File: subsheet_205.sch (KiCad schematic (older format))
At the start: 23 parts, among them U204 TL497A_DIP-14_500MA_PEAK_STEP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, U205 TL497A_DIP-14_500MA_PEAK_STEP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

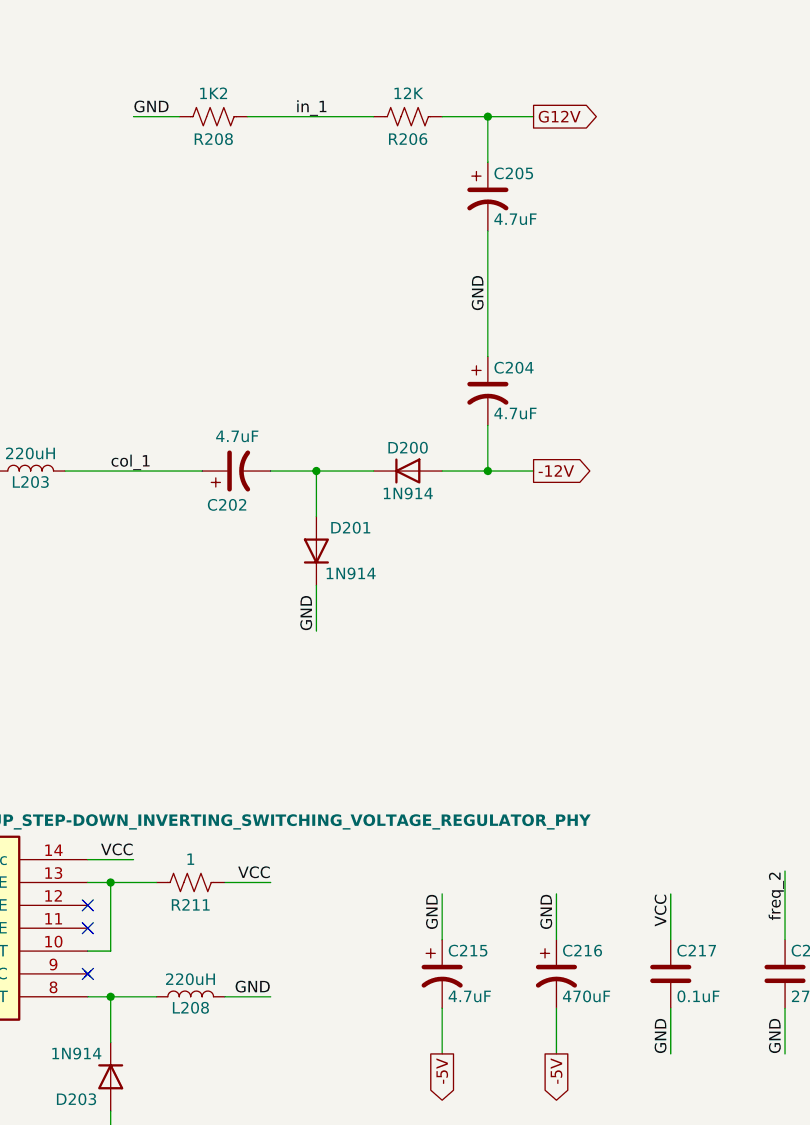
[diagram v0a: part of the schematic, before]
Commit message: Resolves #12 : Use the reference 'CP?' for polarized capacitors
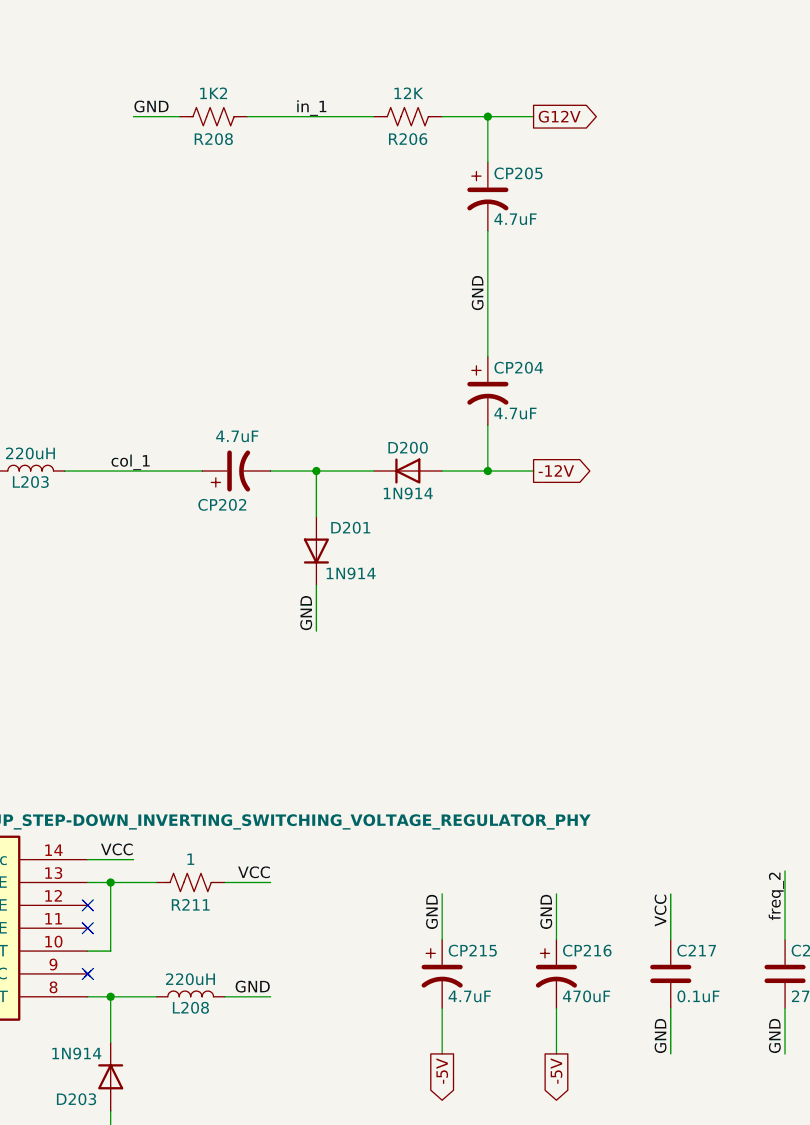
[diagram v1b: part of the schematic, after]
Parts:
- renumbered C202 to CP202, C204 to CP204, C205 to CP205, C215 to CP215, C216 to CP216
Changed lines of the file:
@@
 GND
 $Comp
-L Device:CP1 C205
+L Device:CP1 CP205
 U 1 1 609F4921
 P 5450 2850
-F 0 "C205" H 5475 2950 50  0000 L CNN
+F 0 "CP205" H 5475 2950 50  0000 L CNN
 F 1 "4.7uF" H 5475 2750 50  0000 L CNN
 F 2 "commons_passives_THT:Passive_THT_capacitor_polarized_W5.08mm_L17.78mm" H 5450 2850 50  0001 C CNN
@@
 $EndComp
 $Comp
-L Device:CP1 C204
+L Device:CP1 CP204
 U 1 1 609F43AA
 P 5450 3700
-F 0 "C204" H 5475 3800 50  0000 L CNN
+F 0 "CP204" H 5475 3800 50  0000 L CNN
 F 1 "4.7uF" H 5475 3600 50  0000 L CNN
 F 2 "commons_passives_THT:Passive_THT_capacitor_polarized_W5.08mm_L17.78mm" H 5450 3700 50  0001 C CNN
@@
 	3600 4050 4200 4050
 $Comp
-L Device:CP1 C202
+L Device:CP1 CP202
 U 1 1 609EE420
 P 4350 4050
-F 0 "C202" V 4200 4000 50  0000 L CNN
+F 0 "CP202" V 4200 4000 50  0000 L CNN
 F 1 "4.7uF" V 4500 3950 50  0000 L CNN
 F 2 "commons_passives_THT:Passive_THT_capacitor_polarized_W5.08mm_L17.78mm" H 4350 4050 50  0001 C CNN
@@
 GND
 $Comp
-L Device:CP1 C215
+L Device:CP1 CP215
 U 1 1 60A33402
 P 5250 6250
-F 0 "C215" H 5275 6350 50  0000 L CNN
+F 0 "CP215" H 5275 6350 50  0000 L CNN
 F 1 "4.7uF" H 5275 6150 50  0000 L CNN
 F 2 "commons_passives_THT:Passive_THT_capacitor_polarized_W5.08mm_L17.78mm" H 5250 6250 50  0001 C CNN
@@
 GND
 $Comp
-L Device:CP1 C216
+L Device:CP1 CP216
 U 1 1 60A37D1D
 P 5750 6250
-F 0 "C216" H 5775 6350 50  0000 L CNN
+F 0 "CP216" H 5775 6350 50  0000 L CNN
 F 1 "470uF" H 5775 6150 50  0000 L CNN
 F 2 "commons_passives_THT:Passive_THT_capacitor_polarized_W10.16mm_L27.94mm" H 5750 6250 50  0001 C CNN

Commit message: Resolves #13 : assign 1206 hand-solder footprints to resistors
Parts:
- R203, R206, R208, R211, R213, R214: footprint commons_passives_THT:Passive_THT_resistor_W2.54mm_L12.70mm -> Resistor_SMD:R_1206_3216Metric_Pad1.30x1.75mm_HandSolder
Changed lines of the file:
@@
 F 0 "R208" V 4350 2500 50  0000 C CNN
 F 1 "1K2" V 4150 2500 50  0000 C CNN
-F 2 "commons_passives_THT:Passive_THT_resistor_W2.54mm_L12.70mm" V 4290 2490 50  0001 C CNN
+F 2 "Resistor_SMD:R_1206_3216Metric_Pad1.30x1.75mm_HandSolder" V 4290 2490 50  0001 C CNN
 F 3 "~" H 4250 2500 50  0001 C CNN
 	1    4250 2500
@@
 F 0 "R206" V 5200 2500 50  0000 C CNN
 F 1 "12K" V 5000 2500 50  0000 C CNN
-F 2 "commons_passives_THT:Passive_THT_resistor_W2.54mm_L12.70mm" V 5140 2490 50  0001 C CNN
+F 2 "Resistor_SMD:R_1206_3216Metric_Pad1.30x1.75mm_HandSolder" V 5140 2490 50  0001 C CNN
 F 3 "~" H 5100 2500 50  0001 C CNN
 	1    5100 2500
@@
 F 0 "R203" V 2700 4050 50  0000 C CNN
 F 1 "5.1" V 2500 4050 50  0000 C CNN
-F 2 "commons_passives_THT:Passive_THT_resistor_W2.54mm_L12.70mm" V 2640 4040 50  0001 C CNN
+F 2 "Resistor_SMD:R_1206_3216Metric_Pad1.30x1.75mm_HandSolder" V 2640 4040 50  0001 C CNN
 F 3 "~" H 2600 4050 50  0001 C CNN
 	1    2600 4050
@@
 F 0 "R214" V 2700 7050 50  0000 C CNN
 F 1 "3K9" V 2500 7050 50  0000 C CNN
-F 2 "commons_passives_THT:Passive_THT_resistor_W2.54mm_L12.70mm" V 2640 7040 50  0001 C CNN
+F 2 "Resistor_SMD:R_1206_3216Metric_Pad1.30x1.75mm_HandSolder" V 2640 7040 50  0001 C CNN
 F 3 "~" H 2600 7050 50  0001 C CNN
 	1    2600 7050
@@
 F 0 "R213" V 3550 7050 50  0000 C CNN
 F 1 "1K2" V 3350 7050 50  0000 C CNN
-F 2 "commons_passives_THT:Passive_THT_resistor_W2.54mm_L12.70mm" V 3490 7040 50  0001 C CNN
+F 2 "Resistor_SMD:R_1206_3216Metric_Pad1.30x1.75mm_HandSolder" V 3490 7040 50  0001 C CNN
 F 3 "~" H 3450 7050 50  0001 C CNN
 	1    3450 7050
@@
 F 0 "R211" V 4250 5850 50  0000 C CNN
 F 1 "1" V 4050 5850 50  0000 C CNN
-F 2 "commons_passives_THT:Passive_THT_resistor_W2.54mm_L12.70mm" V 4190 5840 50  0001 C CNN
+F 2 "Resistor_SMD:R_1206_3216Metric_Pad1.30x1.75mm_HandSolder" V 4190 5840 50  0001 C CNN
 F 3 "~" H 4150 5850 50  0001 C CNN
 	1    4150 5850

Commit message: Resolves #8 : Assign 1206 hand-solder footprints to non polarized capacitors
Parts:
- C207, C217: footprint commons_passives_THT:Passive_THT_capacitor_mlcc_W2.54mm_L7.62mm -> Capacitor_SMD:C_1206_3216Metric_Pad1.33x1.80mm_HandSolder
- C208, C209, C218: footprint commons_passives_THT:Passive_THT_capacitor_W2.54mm_L10.16mm -> Capacitor_SMD:C_1206_3216Metric_Pad1.33x1.80mm_HandSolder
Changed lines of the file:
@@
 F 0 "C207" H 5425 1700 50  0000 L CNN
 F 1 "0.1uF" H 5425 1500 50  0000 L CNN
-F 2 "commons_passives_THT:Passive_THT_capacitor_mlcc_W2.54mm_L7.62mm" H 5438 1450 50  0001 C CNN
+F 2 "Capacitor_SMD:C_1206_3216Metric_Pad1.33x1.80mm_HandSolder" H 5438 1450 50  0001 C CNN
 F 3 "~" H 5400 1600 50  0001 C CNN
 	1    5400 1600
@@
 F 0 "C209" H 5925 1700 50  0000 L CNN
 F 1 "330pF" H 5925 1500 50  0000 L CNN
-F 2 "commons_passives_THT:Passive_THT_capacitor_W2.54mm_L10.16mm" H 5938 1450 50  0001 C CNN
+F 2 "Capacitor_SMD:C_1206_3216Metric_Pad1.33x1.80mm_HandSolder" H 5938 1450 50  0001 C CNN
 F 3 "~" H 5900 1600 50  0001 C CNN
 	1    5900 1600
@@
 F 0 "C208" H 2975 4500 50  0000 L CNN
 F 1 "150pF" H 2975 4300 50  0000 L CNN
-F 2 "commons_passives_THT:Passive_THT_capacitor_W2.54mm_L10.16mm" H 2988 4250 50  0001 C CNN
+F 2 "Capacitor_SMD:C_1206_3216Metric_Pad1.33x1.80mm_HandSolder" H 2988 4250 50  0001 C CNN
 F 3 "~" H 2950 4400 50  0001 C CNN
 	1    2950 4400
@@
 F 0 "C217" H 6275 6350 50  0000 L CNN
 F 1 "0.1uF" H 6275 6150 50  0000 L CNN
-F 2 "commons_passives_THT:Passive_THT_capacitor_mlcc_W2.54mm_L7.62mm" H 6288 6100 50  0001 C CNN
+F 2 "Capacitor_SMD:C_1206_3216Metric_Pad1.33x1.80mm_HandSolder" H 6288 6100 50  0001 C CNN
 F 3 "~" H 6250 6250 50  0001 C CNN
 	1    6250 6250
@@
 F 0 "C218" H 6775 6350 50  0000 L CNN
 F 1 "270pF" H 6775 6150 50  0000 L CNN
-F 2 "commons_passives_THT:Passive_THT_capacitor_W2.54mm_L10.16mm" H 6788 6100 50  0001 C CNN
+F 2 "Capacitor_SMD:C_1206_3216Metric_Pad1.33x1.80mm_HandSolder" H 6788 6100 50  0001 C CNN
 F 3 "~" H 6750 6250 50  0001 C CNN
 	1    6750 6250

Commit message: Resolves #9 : Assign radial THT footprints to polarized capacitors
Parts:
- CP202, CP204, CP205, CP215: footprint commons_passives_THT:Passive_THT_capacitor_polarized_W5.08mm_L17.78mm -> Capacitor_THT:C_Radial_D5.0mm_H11.0mm_P2.00mm
- CP216: footprint commons_passives_THT:Passive_THT_capacitor_polarized_W10.16mm_L27.94mm -> Capacitor_THT:C_Radial_D12.5mm_H20.0mm_P5.00mm
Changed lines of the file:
@@
 F 0 "CP205" H 5475 2950 50  0000 L CNN
 F 1 "4.7uF" H 5475 2750 50  0000 L CNN
-F 2 "commons_passives_THT:Passive_THT_capacitor_polarized_W5.08mm_L17.78mm" H 5450 2850 50  0001 C CNN
+F 2 "Capacitor_THT:C_Radial_D5.0mm_H11.0mm_P2.00mm" H 5450 2850 50  0001 C CNN
 F 3 "~" H 5450 2850 50  0001 C CNN
 	1    5450 2850
@@
 F 0 "CP204" H 5475 3800 50  0000 L CNN
 F 1 "4.7uF" H 5475 3600 50  0000 L CNN
-F 2 "commons_passives_THT:Passive_THT_capacitor_polarized_W5.08mm_L17.78mm" H 5450 3700 50  0001 C CNN
+F 2 "Capacitor_THT:C_Radial_D5.0mm_H11.0mm_P2.00mm" H 5450 3700 50  0001 C CNN
 F 3 "~" H 5450 3700 50  0001 C CNN
 	1    5450 3700
@@
 F 0 "CP202" V 4200 4000 50  0000 L CNN
 F 1 "4.7uF" V 4500 3950 50  0000 L CNN
-F 2 "commons_passives_THT:Passive_THT_capacitor_polarized_W5.08mm_L17.78mm" H 4350 4050 50  0001 C CNN
+F 2 "Capacitor_THT:C_Radial_D5.0mm_H11.0mm_P2.00mm" H 4350 4050 50  0001 C CNN
 F 3 "~" H 4350 4050 50  0001 C CNN
 	1    4350 4050
@@
 F 0 "CP215" H 5275 6350 50  0000 L CNN
 F 1 "4.7uF" H 5275 6150 50  0000 L CNN
-F 2 "commons_passives_THT:Passive_THT_capacitor_polarized_W5.08mm_L17.78mm" H 5250 6250 50  0001 C CNN
+F 2 "Capacitor_THT:C_Radial_D5.0mm_H11.0mm_P2.00mm" H 5250 6250 50  0001 C CNN
 F 3 "~" H 5250 6250 50  0001 C CNN
 	1    5250 6250
@@
 F 0 "CP216" H 5775 6350 50  0000 L CNN
 F 1 "470uF" H 5775 6150 50  0000 L CNN
-F 2 "commons_passives_THT:Passive_THT_capacitor_polarized_W10.16mm_L27.94mm" H 5750 6250 50  0001 C CNN
+F 2 "Capacitor_THT:C_Radial_D12.5mm_H20.0mm_P5.00mm" H 5750 6250 50  0001 C CNN
 F 3 "~" H 5750 6250 50  0001 C CNN
 	1    5750 6250

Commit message: Resolves #16 : assign smd footprints to diodes
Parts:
- D200, D201, D203: footprint commons_passives_THT:Passive_THT_diode_W2.54mm_L12.70mm -> Diode_SMD:D_SOD-123F
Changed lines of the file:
@@
 F 0 "D201" V 4800 4250 50  0000 C CNN
 F 1 "1N914" V 4600 4250 50  0000 C CNN
-F 2 "commons_passives_THT:Passive_THT_diode_W2.54mm_L12.70mm" H 4700 4400 50  0001 C CNN
+F 2 "Diode_SMD:D_SOD-123F" H 4700 4400 50  0001 C CNN
 F 3 "~" H 4700 4400 50  0001 C CNN
 	1    4700 4400
@@
 F 0 "D200" H 5100 4150 50  0000 C CNN
 F 1 "1N914" H 5100 3950 50  0000 C CNN
-F 2 "commons_passives_THT:Passive_THT_diode_W2.54mm_L12.70mm" H 5100 4050 50  0001 C CNN
+F 2 "Diode_SMD:D_SOD-123F" H 5100 4050 50  0001 C CNN
 F 3 "~" H 5100 4050 50  0001 C CNN
 	1    5100 4050
@@
 F 0 "D203" V 3900 6550 50  0000 C CNN
 F 1 "1N914" V 3700 6550 50  0000 C CNN
-F 2 "commons_passives_THT:Passive_THT_diode_W2.54mm_L12.70mm" H 3800 6700 50  0001 C CNN
+F 2 "Diode_SMD:D_SOD-123F" H 3800 6700 50  0001 C CNN
 F 3 "~" H 3800 6700 50  0001 C CNN
 	1    3800 6700

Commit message: Resolves #15 : assign smd footprints to the inductors
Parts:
- L203, L208: footprint commons_passives_THT:Passive_THT_inductor_W5.08mm_L15.24mm -> commons-passives_SMD:L_Bourns_SRR1208
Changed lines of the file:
@@
 F 0 "L203" V 3400 4050 50  0000 C CNN
 F 1 "220uH" V 3525 4050 50  0000 C CNN
-F 2 "commons_passives_THT:Passive_THT_inductor_W5.08mm_L15.24mm" H 3450 4050 50  0001 C CNN
+F 2 "commons-passives_SMD:L_Bourns_SRR1208" H 3450 4050 50  0001 C CNN
 F 3 "~" H 3450 4050 50  0001 C CNN
 	1    3450 4050
@@
 F 0 "L208" V 4100 6350 50  0000 C CNN
 F 1 "220uH" V 4225 6350 50  0000 C CNN
-F 2 "commons_passives_THT:Passive_THT_inductor_W5.08mm_L15.24mm" H 4150 6350 50  0001 C CNN
+F 2 "commons-passives_SMD:L_Bourns_SRR1208" H 4150 6350 50  0001 C CNN
 F 3 "~" H 4150 6350 50  0001 C CNN
 	1    4150 6350
